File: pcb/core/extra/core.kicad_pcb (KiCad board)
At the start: 2 copper layers, 79.3 x 78.9 mm, 7 parts, among them J1 Conn_01x11, J2 Conn_01x11, U1 Helios

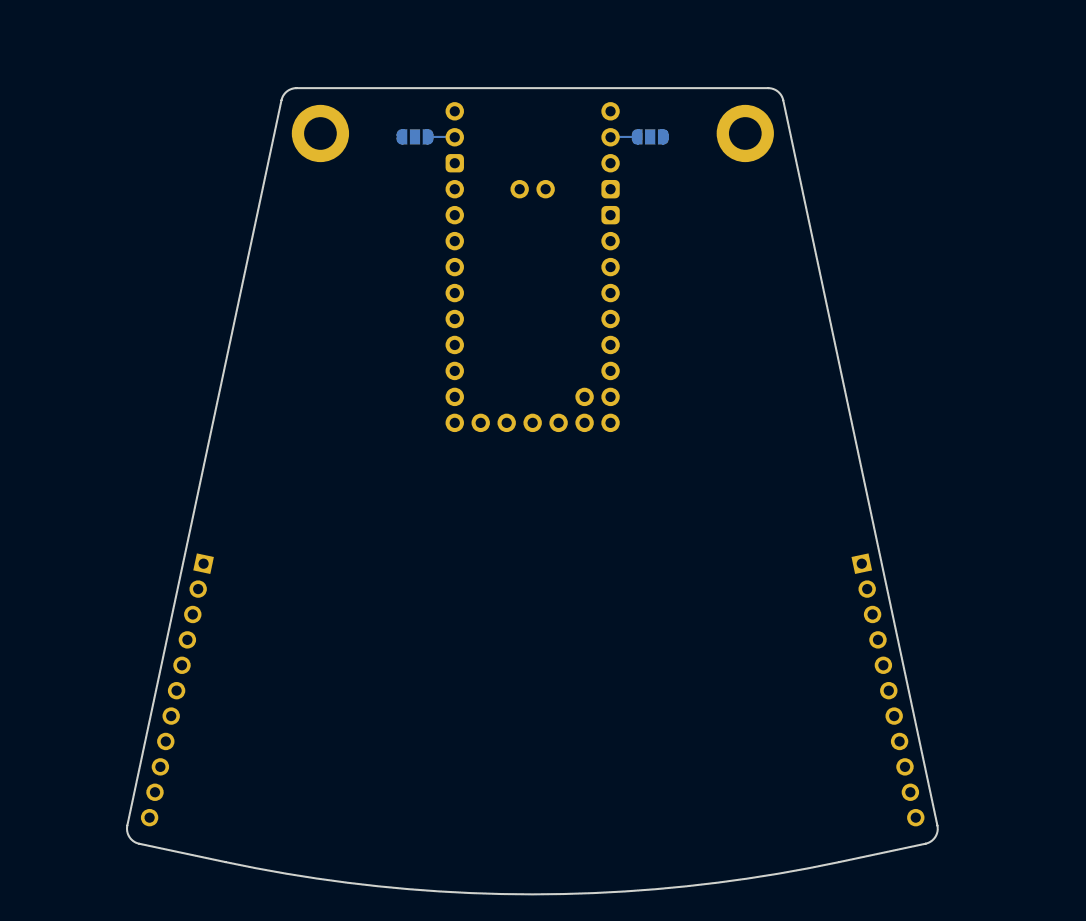
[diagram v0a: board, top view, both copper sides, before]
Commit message: moved rgb jumpers to the other side
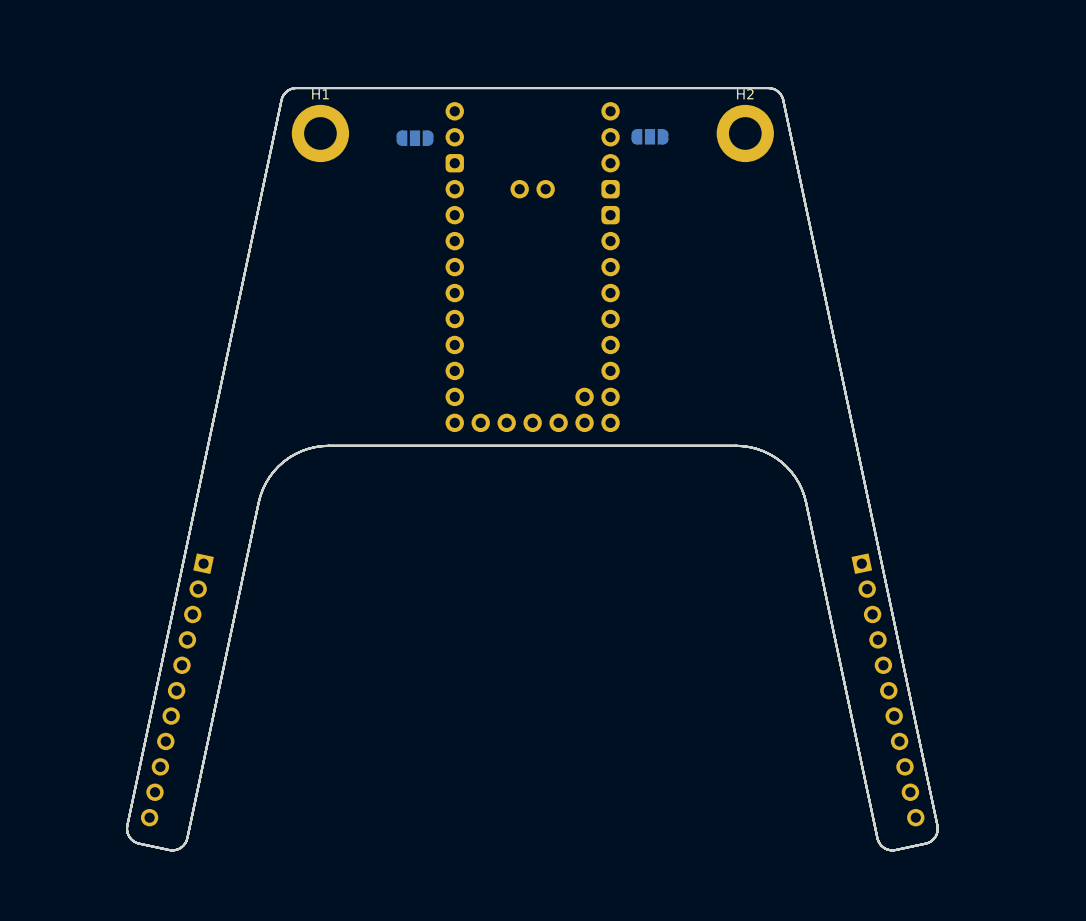
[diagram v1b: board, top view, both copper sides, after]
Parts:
- moved JP2 0.13 mm to (186.7, 139.3)
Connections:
- net 5V renamed Net-(JP2-A)
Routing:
- net Net-(JP2-A): track 2.61 -> 0.00 mm
- net Net-(JP1-B): track 2.69 -> 0.08 mm
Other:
- board size 79.3 x 78.9 mm -> 79.3 x 74.6 mm

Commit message: finished extra core pcb
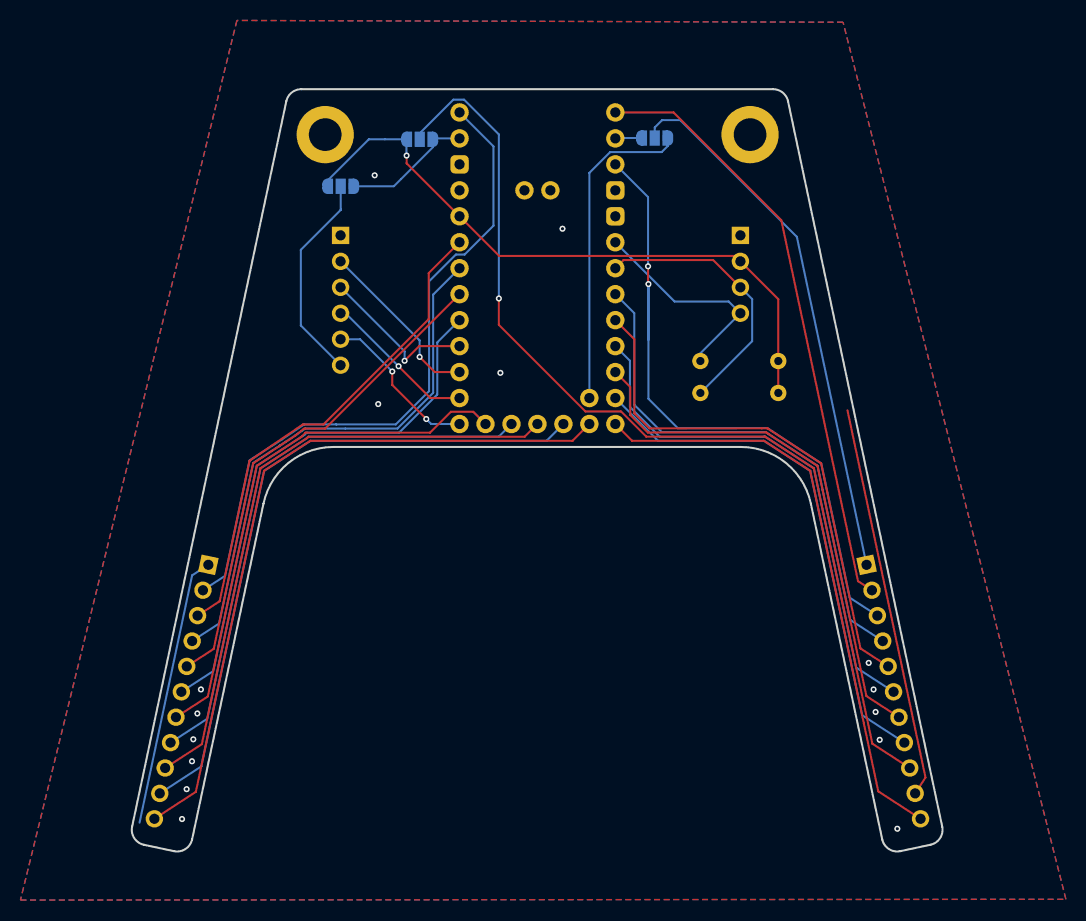
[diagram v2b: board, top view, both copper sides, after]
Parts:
- added J3: I2C, Connector_PinHeader_2.54mm:PinHeader_1x04_P2.54mm_Vertical, B.Cu at (218.5, 148.8)
- added J4: SPI, Connector_PinHeader_2.54mm:PinHeader_1x06_P2.54mm_Vertical, B.Cu at (179.4, 148.8)
- added JP3: Jumper_3_Open, Jumper:SolderJumper-3_P1.3mm_Open_RoundedPad1.0x1.5mm, B.Cu at (179.4, 144.0)
- added R1: 4.7k, Resistor_THT:R_Axial_DIN0207_L6.3mm_D2.5mm_P7.62mm_Horizontal, B.Cu at (222.2, 161.1)
- added R2: 4.7k, Resistor_THT:R_Axial_DIN0207_L6.3mm_D2.5mm_P7.62mm_Horizontal, B.Cu at (222.2, 164.2)
- moved H1 0.48 mm to (177.9, 139.0)
- moved U1 0.48 mm to (198.7, 153.3)
- moved JP1 0.48 mm to (210.1, 139.3)
- moved J1 0.48 mm to (166.5, 181.1)
- moved JP2 0.48 mm to (187.2, 139.4)
- moved H2 0.48 mm to (219.5, 139.0)
- moved J2 0.48 mm to (230.9, 181.1)
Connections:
- net Net-(JP2-A) renamed 5V
- U1 pad 21: unconnected-(U1-P22-Pad21) -> sck
- U1 pad 22: unconnected-(U1-P20-Pad22) -> miso
- U1 pad 23: unconnected-(U1-P23-Pad23) -> mosi
- U1 pad 24: unconnected-(U1-P21-Pad24) -> cs
- U1 pad 5: unconnected-(U1-P2-Pad5) -> sda
- U1 pad 6: unconnected-(U1-P3-Pad6) -> scl
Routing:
- net vccrgb: track 0.00 -> 97.9 mm, vias 0 -> 1
- net row3: track 0.00 -> 70.3 mm
- net col0: track 0.00 -> 65.8 mm
- net col11: track 0.00 -> 65.5 mm, vias 0 -> 2
- net row2: track 0.00 -> 65.2 mm
- net GND: track 0.00 -> 65.2 mm, vias 0 -> 15
- net vcc: track 0.00 -> 63.4 mm, vias 0 -> 1
- net row1: track 0.00 -> 60.4 mm
- net row5: track 0.00 -> 58.3 mm
- net row4: track 0.00 -> 57.6 mm
- net row0: track 0.00 -> 55.3 mm
- net rgb: track 0.00 -> 52.8 mm
- net col4: track 0.00 -> 52.6 mm
- net col2: track 0.00 -> 52.5 mm
- net col7: track 0.00 -> 51.6 mm
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- added copper zone on B.Cu, net GND
- added copper zone on F.Cu, net GND
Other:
- board text added: "CS"
- board text added: "GND"
- board text added: "MISO"
- board text added: "MOSI"
- board text added: "SCK"
- board text added: "SCL"
- board text added: "SDA"
- board text added: "SPI"
- board text added: "VCC"
